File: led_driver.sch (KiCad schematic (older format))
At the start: 3 parts, among them P1 CONN_01X02, U1 AL5809-15P1-7

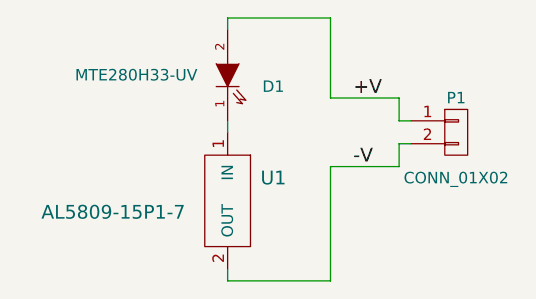
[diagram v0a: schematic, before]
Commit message: Update silk screen
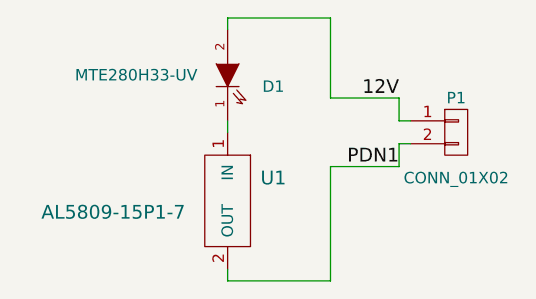
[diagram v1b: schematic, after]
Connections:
- net +V renamed 12V
- net -V renamed PDN1
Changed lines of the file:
@@
 	1    0    0    -1
 $EndComp
-Text Label 6600 3150 0    60   ~ 0
-+V
-Text Label 6600 3450 0    60   ~ 0
--V
+Text Label 6800 3150 2    60   ~ 0
+12V
+Text Label 6800 3450 2    60   ~ 0
+PDN1
 Wire Wire Line
 	6050 3950 6050 3900
